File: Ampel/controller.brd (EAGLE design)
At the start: 100 x 80 mm, 9 parts, among them IC1 ATtiny25, J1 J5MM, X1 22-23-2041

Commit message: spannungsregler
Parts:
- removed J1: J5MM, jumper:05
- added C2: (no value), resistor:C025-024X044
- added C3: (no value), resistor:E5-4
- added D1, D2: 1N4004, diode:DO41-10
- added IC2: 7805L, linear:TO92
- added X2: KUSBVX, con-kycon:KUSBVX
- moved SV1 2.54 mm to (39.4, 55.9)
- moved OUT1 1.27 mm to (33.0, 67.3), turned to 90 degrees
- moved OUT2 1.27 mm to (24.1, 67.3), turned to 90 degrees
- moved X1 1.27 mm to (43.2, 67.3)
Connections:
- removed net VDD: OUT1.3, OUT2.3, X1.1
- new net VEE: C3.+, D1.C, IC2.3
- net GND: now also C2.2, C3.-, D2.A, IC2.2, X2.4
- net VCC: now also C2.1, D1.A, D2.C, IC2.1, OUT1.3, OUT2.3, X2.1; no longer J1.1, J1.2
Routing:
- net GND: track 0.00 -> 85.1 mm
- net VCC: track 80.0 -> 111.8 mm
- net VDD: track 24.1 -> 0.00 mm
- net MISO: track 26.7 -> 30.5 mm
- net SCK: track 41.9 -> 39.4 mm
- net RESET: track 44.5 -> 41.9 mm
- net MOSI: track 20.3 -> 21.6 mm

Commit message: some routing
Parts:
- moved D2 43.8 mm to (14.0, 15.2), turned to 90 degrees
- moved X2 43.2 mm to (10.2, 5.08), turned to 180 degrees
- moved C1 38.2 mm to (20.3, 20.3)
- moved IC1 38.2 mm to (26.7, 17.8)
- moved IN 38.2 mm to (26.7, 6.35)
- moved OUT1 38.2 mm to (30.5, 29.2)
- moved OUT2 38.2 mm to (21.6, 29.2)
- moved SV1 38.2 mm to (36.8, 17.8)
- moved X1 38.2 mm to (40.6, 29.2)
- moved R1 38.2 mm to (20.3, 10.2)
- moved C3 37.6 mm to (11.4, 22.9)
- moved C2 37.0 mm to (12.7, 26.7)
- moved D1 35.7 mm to (8.89, 15.2), turned to 270 degrees
- moved IC2 34.9 mm to (10.2, 30.5), turned to 270 degrees
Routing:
- net VCC: track 111.8 -> 179.4 mm
- net GND: track 85.1 -> 124.5 mm
- net VEE: track 0.00 -> 9.42 mm
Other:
- board size 100 x 80 mm -> 47.9 x 35.5 mm

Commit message: some routing
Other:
- board size 47.9 x 35.5 mm -> 80 x 35 mm
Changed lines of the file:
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@@
 <setting verticaltext="up"/>
 </settings>
-<grid distance="0.05" unitdist="inch" unit="inch" style="lines" multiple="1" display="no" altdistance="0.025" altunitdist="inch" altunit="inch"/>
+<grid distance="1" unitdist="mm" unit="mm" style="lines" multiple="1" display="no" altdistance="0.025" altunitdist="inch" altunit="inch"/>
 <layers>
 <layer number="1" name="Top" color="4" fill="1" visible="yes" active="yes"/>
@@
 <layer number="43" name="vRestrict" color="2" fill="10" visible="yes" active="yes"/>
 <layer number="44" name="Drills" color="7" fill="1" visible="no" active="yes"/>
-<layer number="45" name="Holes" color="7" fill="1" visible="no" active="yes"/>
+<layer number="45" name="Holes" color="7" fill="1" visible="yes" active="yes"/>
 <layer number="46" name="Milling" color="3" fill="1" visible="no" active="yes"/>
 <layer number="47" name="Measures" color="7" fill="1" visible="no" active="yes"/>
@@
 <board>
 <plain>
-<wire x1="0" y1="0" x2="47.93" y2="0" width="0" layer="20"/>
-<wire x1="47.93" y1="0" x2="47.93" y2="35.55" width="0" layer="20"/>
-<wire x1="47.93" y1="35.55" x2="0" y2="35.55" width="0" layer="20"/>
-<wire x1="0" y1="35.55" x2="0" y2="0" width="0" layer="20"/>
+<wire x1="0" y1="0" x2="80" y2="0" width="0" layer="20"/>
+<wire x1="80" y1="0" x2="80" y2="35" width="0" layer="20"/>
+<wire x1="80" y1="35" x2="0" y2="35" width="0" layer="20"/>
+<wire x1="0" y1="35" x2="0" y2="0" width="0" layer="20"/>
+<hole x="65" y="10" drill="10"/>
 </plain>
 <attributes>

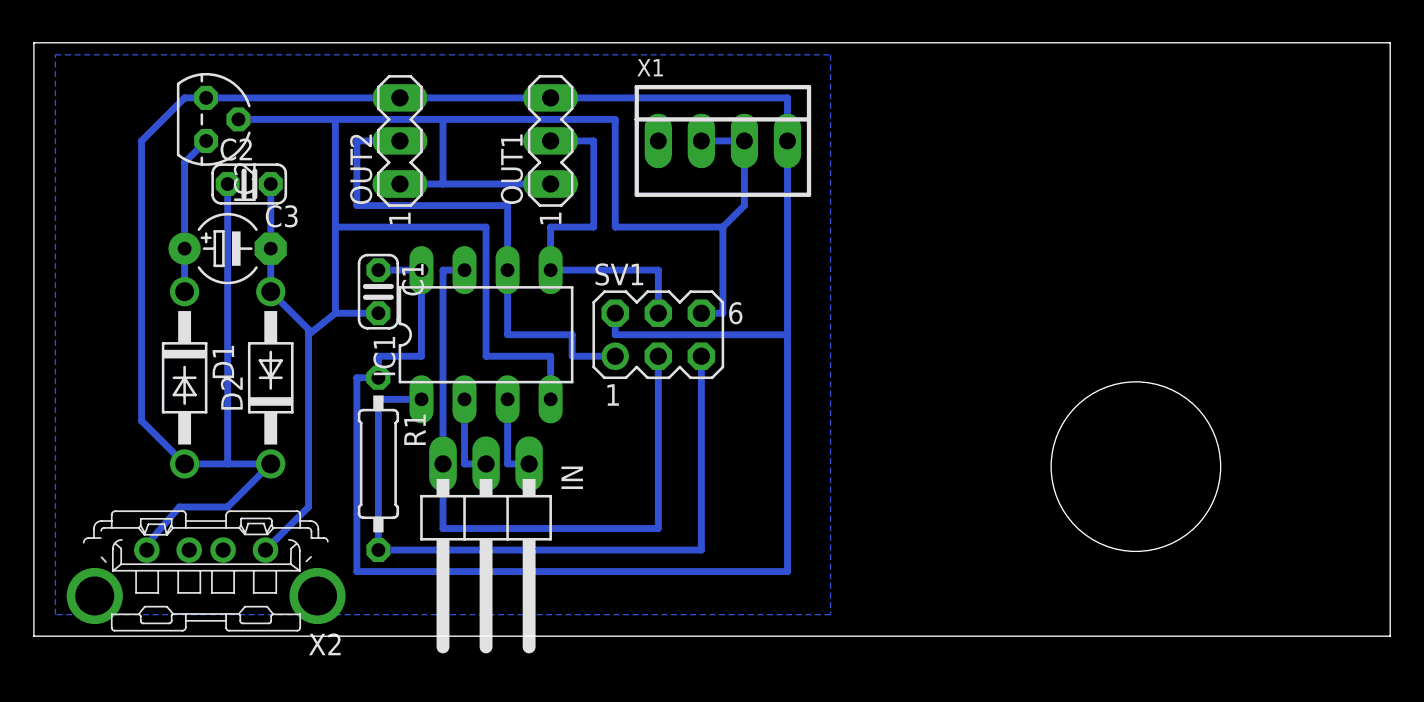
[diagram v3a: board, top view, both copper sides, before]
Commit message: Jumper für Stromversorgung und Spannungsregler angepasst
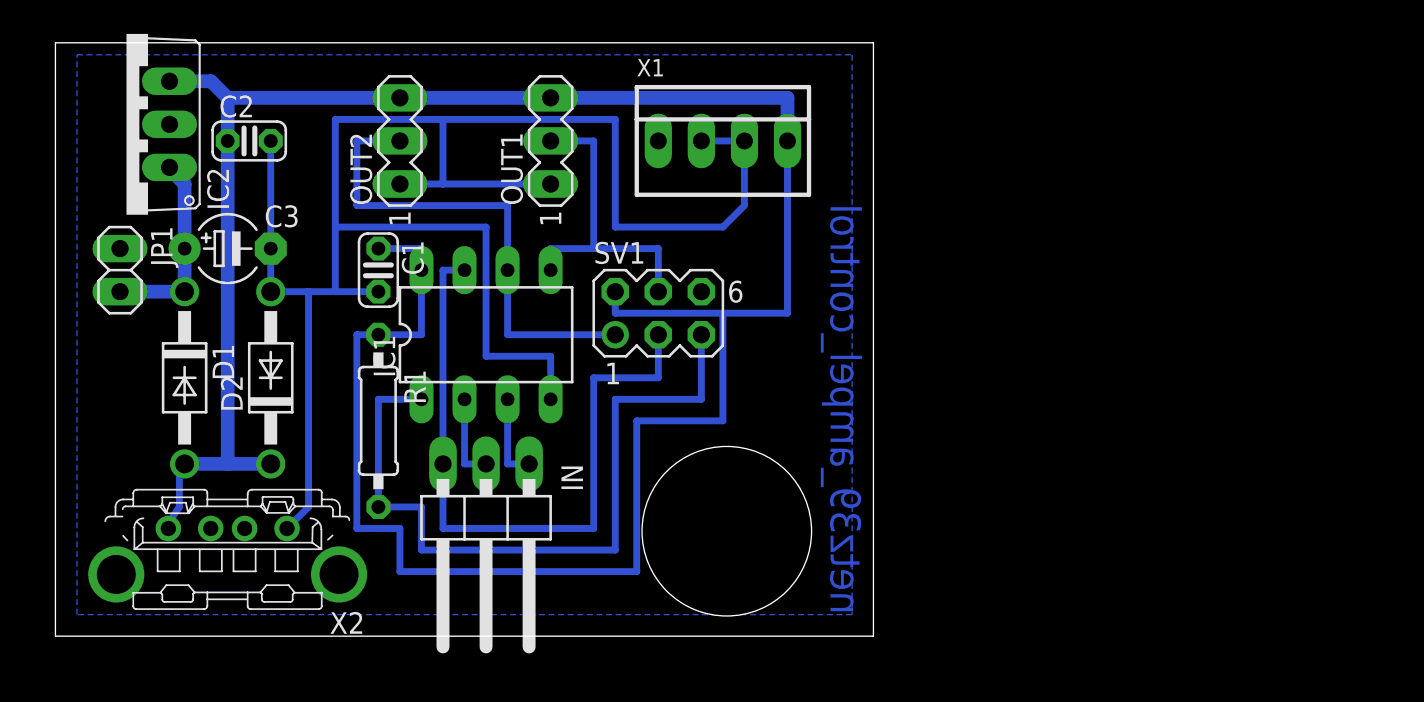
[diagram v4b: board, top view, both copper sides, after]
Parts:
- added JP1: (no value), pinhead:1X02
- C2: value (none) -> 0.1µ
- C3: value (none) -> 470µ
- IC2: value 7805L -> 7805TV; device linear:TO92 -> linear:TO220V
- moved IC2 4.71 mm to (5.46, 30.2), turned to 90 degrees
- moved C2 2.54 mm to (12.7, 29.2)
- moved R1 2.54 mm to (20.3, 12.7)
- moved X2 1.80 mm to (11.4, 6.35)
- moved C1 1.27 mm to (20.3, 21.6)
- moved SV1 1.27 mm to (36.8, 19.1)
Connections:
- net GND: now also JP1.1
- net VCC: now also IC2.3; no longer IC2.1
- net VEE: now also IC2.1, JP1.2; no longer IC2.3
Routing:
- net VCC: track 179.4 -> 154.0 mm
- net GND: track 124.5 -> 112.8 mm
- net MOSI: track 21.6 -> 19.1 mm
- net VEE: track 9.42 -> 11.5 mm
- net RESET: track 41.9 -> 43.2 mm
- net MISO: track 30.5 -> 29.2 mm
- net SCK: track 39.4 -> 40.6 mm
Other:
- board size 80 x 35 mm -> 48.2 x 35 mm
- board text added: "netz39_ampel_control"

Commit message: Ladekondensatoren angepasst
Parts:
- C3: value 470µ -> 47µ
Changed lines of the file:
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@@
 <element name="IN" library="pinhead" package="1X03/90" value="" x="26.67" y="6.35" rot="R180"/>
 <element name="C2" library="resistor" package="C025-024X044" value="0.1µ" x="12.7" y="29.21"/>
-<element name="C3" library="resistor" package="E5-4" value="470µ" x="11.43" y="22.86"/>
+<element name="C3" library="resistor" package="E5-4" value="47µ" x="11.43" y="22.86"/>
 <element name="D1" library="diode" package="DO41-10" value="1N4004" x="8.89" y="15.24" rot="R270"/>
 <element name="D2" library="diode" package="DO41-10" value="1N4004" x="13.97" y="15.24" rot="R90"/>
